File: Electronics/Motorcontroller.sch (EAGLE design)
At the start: 27 parts, among them Q1 IRFZ48V, Q2 IRF4905V, Q3 IRFZ48V, Q4 IRF4905V, Q5 IRFZ48V, Q6 IRF4905V, Q7 IRFZ48V, Q8 IRF4905V, X3 24V Batt

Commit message: Motorboard v2.0
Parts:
- added LED2, LED3, LED4, LED5: (no value), led:LED3MM
- added R7, R8: 2.2k, rcl:R-EU_0207/10
- LED1: device led:LED5MM -> led:LED3MM
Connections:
- removed net N$1: Q5.D, Q6.D, X2-2.KL
- new net N$23: LED2.C, LED3.A, R7.2
- new net N$24: LED4.A, LED5.C, R8.2
- new net N$25: LED4.C, LED5.A, Q5.D, Q6.D, X2-2.KL
- net N$18: now also R8.1
- net N$2: now also R7.1
- net N$4: now also LED2.A, LED3.C
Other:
- moved on the sheet: X1-1, X1-2, X2-1, X2-2
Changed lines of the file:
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@@
 <?xml version="1.0" encoding="utf-8"?>
 <!DOCTYPE eagle SYSTEM "eagle.dtd">
-<eagle version="6.0">
+<eagle version="6.1">
 <drawing>
 <settings>
@@
 <part name="P+5" library="supply1" deviceset="+24V" device=""/>
 <part name="R13" library="rcl" deviceset="R-EU_" device="0207/10" value="1k"/>
-<part name="LED1" library="led" deviceset="LED" device="5MM"/>
+<part name="LED1" library="led" deviceset="LED" device="3MM"/>
 <part name="OK1" library="optocoupler" deviceset="4N35" device=""/>
 <part name="OK2" library="optocoupler" deviceset="4N35" device=""/>
@@
 <part name="GND1" library="supply1" deviceset="GND" device=""/>
 <part name="C1" library="rcl" deviceset="CPOL-EU" device="E5-13" value="2200µF"/>
+<part name="LED2" library="led" deviceset="LED" device="3MM"/>
+<part name="LED3" library="led" deviceset="LED" device="3MM"/>
+<part name="R7" library="rcl" deviceset="R-EU_" device="0207/10" value="2.2k"/>
+<part name="LED4" library="led" deviceset="LED" device="3MM"/>
+<part name="LED5" library="led" deviceset="LED" device="3MM"/>
+<part name="R8" library="rcl" deviceset="R-EU_" device="0207/10" value="2.2k"/>
 </parts>
 <sheets>
@@
 <instance part="Q3" gate="G$1" x="190.5" y="93.98"/>
 <instance part="Q4" gate="G$1" x="190.5" y="109.22"/>
-<instance part="X1" gate="-1" x="226.06" y="101.6" rot="R180"/>
-<instance part="X1" gate="-2" x="226.06" y="104.14" rot="R180"/>
+<instance part="X1" gate="-1" x="246.38" y="101.6" rot="R180"/>
+<instance part="X1" gate="-2" x="246.38" y="104.14" rot="R180"/>
 <instance part="Q1" gate="G$1" x="215.9" y="93.98"/>
 <instance part="Q2" gate="G$1" x="215.9" y="109.22"/>
@@
 <instance part="Q5" gate="G$1" x="190.5" y="45.72"/>
 <instance part="Q6" gate="G$1" x="190.5" y="60.96"/>
-<instance part="X2" gate="-1" x="226.06" y="53.34" rot="R180"/>
-<instance part="X2" gate="-2" x="226.06" y="55.88" rot="R180"/>
+<instance part="X2" gate="-1" x="246.38" y="53.34" rot="R180"/>
+<instance part="X2" gate="-2" x="246.38" y="55.88" rot="R180"/>
 <instance part="Q7" gate="G$1" x="215.9" y="45.72"/>
 <instance part="Q8" gate="G$1" x="215.9" y="63.5"/>
@@
 <instance part="GND1" gate="1" x="142.24" y="68.58"/>
 <instance part="C1" gate="G$1" x="185.42" y="160.02"/>
+<instance part="LED2" gate="G$1" x="236.22" y="124.46"/>
+<instance part="LED3" gate="G$1" x="228.6" y="121.92" rot="R180"/>
+<instance part="R7" gate="G$1" x="236.22" y="111.76" rot="R90"/>
+<instance part="LED4" gate="G$1" x="228.6" y="73.66" rot="R180"/>
+<instance part="LED5" gate="G$1" x="236.22" y="76.2"/>
+<instance part="R8" gate="G$1" x="236.22" y="63.5" rot="R90"/>
 </instances>
 <busses>
@@
 <pinref part="X1" gate="-1" pin="KL"/>
 <wire x1="193.04" y1="101.6" x2="193.04" y2="99.06" width="0.1524" layer="91"/>
-<wire x1="220.98" y1="101.6" x2="193.04" y2="101.6" width="0.1524" layer="91"/>
+<wire x1="241.3" y1="101.6" x2="236.22" y2="101.6" width="0.1524" layer="91"/>
 <junction x="193.04" y="101.6"/>
+<pinref part="R7" gate="G$1" pin="1"/>
+<wire x1="236.22" y1="101.6" x2="193.04" y2="101.6" width="0.1524" layer="91"/>
+<wire x1="236.22" y1="106.68" x2="236.22" y2="101.6" width="0.1524" layer="91"/>
+<junction x="236.22" y="101.6"/>
 </segment>
 </net>
@@
 <wire x1="218.44" y1="104.14" x2="218.44" y2="99.06" width="0.1524" layer="91"/>
 <pinref part="X1" gate="-2" pin="KL"/>
-<wire x1="220.98" y1="104.14" x2="218.44" y2="104.14" width="0.1524" layer="91"/>
+<wire x1="241.3" y1="104.14" x2="238.76" y2="104.14" width="0.1524" layer="91"/>
 <junction x="218.44" y="104.14"/>
+<wire x1="238.76" y1="104.14" x2="218.44" y2="104.14" width="0.1524" layer="91"/>
+<wire x1="238.76" y1="104.14" x2="238.76" y2="129.54" width="0.1524" layer="91"/>
+<junction x="238.76" y="104.14"/>
+<pinref part="LED3" gate="G$1" pin="C"/>
+<wire x1="228.6" y1="127" x2="228.6" y2="129.54" width="0.1524" layer="91"/>
+<wire x1="228.6" y1="129.54" x2="236.22" y2="129.54" width="0.1524" layer="91"/>
+<pinref part="LED2" gate="G$1" pin="A"/>
+<wire x1="236.22" y1="129.54" x2="238.76" y2="129.54" width="0.1524" layer="91"/>
+<wire x1="236.22" y1="127" x2="236.22" y2="129.54" width="0.1524" layer="91"/>
+<junction x="236.22" y="129.54"/>
 </segment>
 </net>
@@
 </segment>
 </net>
-<net name="N$1" class="0">
-<segment>
-<pinref part="Q5" gate="G$1" pin="D"/>
-<pinref part="Q6" gate="G$1" pin="D"/>
-<wire x1="193.04" y1="55.88" x2="193.04" y2="50.8" width="0.1524" layer="91"/>
-<pinref part="X2" gate="-2" pin="KL"/>
-<wire x1="220.98" y1="55.88" x2="193.04" y2="55.88" width="0.1524" layer="91"/>
-<junction x="193.04" y="55.88"/>
-</segment>
-</net>
 <net name="N$18" class="0">
 <segment>
@@
 <pinref part="X2" gate="-1" pin="KL"/>
 <wire x1="218.44" y1="53.34" x2="218.44" y2="50.8" width="0.1524" layer="91"/>
-<wire x1="220.98" y1="53.34" x2="218.44" y2="53.34" width="0.1524" layer="91"/>
+<wire x1="241.3" y1="53.34" x2="236.22" y2="53.34" width="0.1524" layer="91"/>
 <junction x="218.44" y="53.34"/>
+<pinref part="R8" gate="G$1" pin="1"/>
+<wire x1="236.22" y1="53.34" x2="218.44" y2="53.34" width="0.1524" layer="91"/>
+<wire x1="236.22" y1="58.42" x2="236.22" y2="53.34" width="0.1524" layer="91"/>
+<junction x="236.22" y="53.34"/>
 </segment>
 </net>
@@
 </segment>
 </net>
+<net name="N$23" class="0">
+<segment>
+<pinref part="LED3" gate="G$1" pin="A"/>
+<wire x1="228.6" y1="119.38" x2="228.6" y2="116.84" width="0.1524" layer="91"/>
+<pinref part="R7" gate="G$1" pin="2"/>
+<wire x1="228.6" y1="116.84" x2="236.22" y2="116.84" width="0.1524" layer="91"/>
+<pinref part="LED2" gate="G$1" pin="C"/>
+<wire x1="236.22" y1="119.38" x2="236.22" y2="116.84" width="0.1524" layer="91"/>
+<junction x="236.22" y="116.84"/>
+</segment>
+</net>
+<net name="N$24" class="0">
+<segment>
+<pinref part="R8" gate="G$1" pin="2"/>
+<pinref part="LED5" gate="G$1" pin="C"/>
+<wire x1="236.22" y1="68.58" x2="236.22" y2="71.12" width="0.1524" layer="91"/>
+<pinref part="LED4" gate="G$1" pin="A"/>
+<wire x1="236.22" y1="68.58" x2="228.6" y2="68.58" width="0.1524" layer="91"/>
+<wire x1="228.6" y1="68.58" x2="228.6" y2="71.12" width="0.1524" layer="91"/>
+<junction x="236.22" y="68.58"/>
+</segment>
+</net>
+<net name="N$25" class="0">
+<segment>
+<pinref part="LED4" gate="G$1" pin="C"/>
+<wire x1="228.6" y1="78.74" x2="228.6" y2="81.28" width="0.1524" layer="91"/>
+<wire x1="238.76" y1="81.28" x2="236.22" y2="81.28" width="0.1524" layer="91"/>
+<pinref part="LED5" gate="G$1" pin="A"/>
+<wire x1="236.22" y1="81.28" x2="228.6" y2="81.28" width="0.1524" layer="91"/>
+<wire x1="236.22" y1="78.74" x2="236.22" y2="81.28" width="0.1524" layer="91"/>
+<junction x="236.22" y="81.28"/>
+<pinref part="Q5" gate="G$1" pin="D"/>
+<pinref part="Q6" gate="G$1" pin="D"/>
+<wire x1="193.04" y1="55.88" x2="193.04" y2="50.8" width="0.1524" layer="91"/>
+<pinref part="X2" gate="-2" pin="KL"/>
+<wire x1="241.3" y1="55.88" x2="238.76" y2="55.88" width="0.1524" layer="91"/>
+<junction x="193.04" y="55.88"/>
+<wire x1="238.76" y1="55.88" x2="193.04" y2="55.88" width="0.1524" layer="91"/>
+<wire x1="238.76" y1="81.28" x2="238.76" y2="55.88" width="0.1524" layer="91"/>
+<junction x="238.76" y="55.88"/>
+</segment>
+</net>

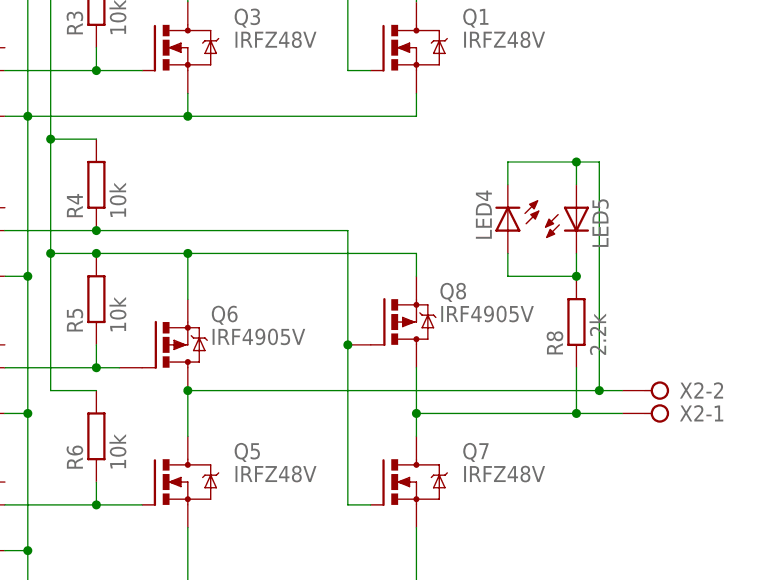
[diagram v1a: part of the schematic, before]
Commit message: Updated .sch to be consisting to .brd (it was missing from the last commit)
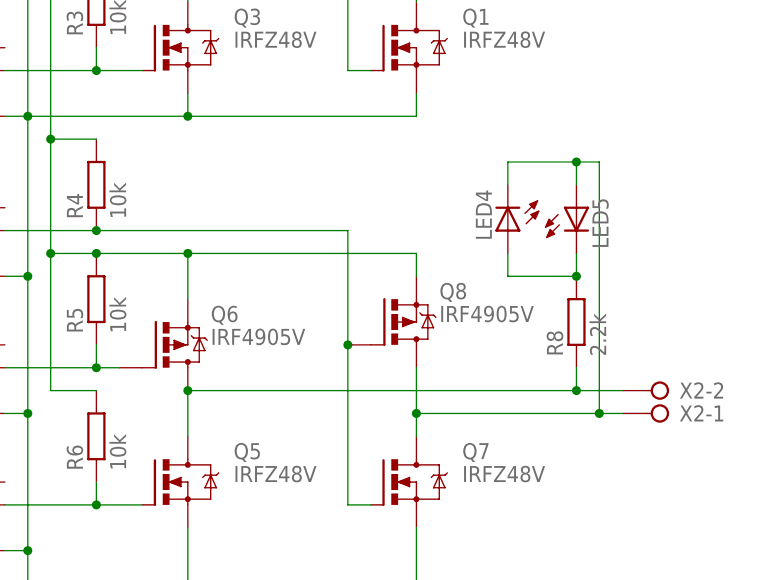
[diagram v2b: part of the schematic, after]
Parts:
- R7, R8: device rcl:R-EU_0207/10 -> rcl:R-EU_0207/7
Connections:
- removed net N$18: Q7.D, Q8.D, R8.1, X2-1.KL
- new net N$1: LED4.C, LED5.A, Q7.D, Q8.D, X2-1.KL
- net N$25: now also R8.1; no longer LED4.C, LED5.A
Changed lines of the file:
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@@
 <part name="LED2" library="led" deviceset="LED" device="3MM"/>
 <part name="LED3" library="led" deviceset="LED" device="3MM"/>
-<part name="R7" library="rcl" deviceset="R-EU_" device="0207/10" value="2.2k"/>
+<part name="R7" library="rcl" deviceset="R-EU_" device="0207/7" value="2.2k"/>
 <part name="LED4" library="led" deviceset="LED" device="3MM"/>
 <part name="LED5" library="led" deviceset="LED" device="3MM"/>
-<part name="R8" library="rcl" deviceset="R-EU_" device="0207/10" value="2.2k"/>
+<part name="R8" library="rcl" deviceset="R-EU_" device="0207/7" value="2.2k"/>
 </parts>
 <sheets>
@@
 </segment>
 </net>
-<net name="N$18" class="0">
-<segment>
-<pinref part="Q8" gate="G$1" pin="D"/>
-<pinref part="Q7" gate="G$1" pin="D"/>
-<wire x1="218.44" y1="58.42" x2="218.44" y2="53.34" width="0.1524" layer="91"/>
-<pinref part="X2" gate="-1" pin="KL"/>
-<wire x1="218.44" y1="53.34" x2="218.44" y2="50.8" width="0.1524" layer="91"/>
-<wire x1="241.3" y1="53.34" x2="236.22" y2="53.34" width="0.1524" layer="91"/>
-<junction x="218.44" y="53.34"/>
-<pinref part="R8" gate="G$1" pin="1"/>
-<wire x1="236.22" y1="53.34" x2="218.44" y2="53.34" width="0.1524" layer="91"/>
-<wire x1="236.22" y1="58.42" x2="236.22" y2="53.34" width="0.1524" layer="91"/>
-<junction x="236.22" y="53.34"/>
-</segment>
-</net>
 <net name="N$19" class="0">
 <segment>
@@
 <net name="N$25" class="0">
 <segment>
-<pinref part="LED4" gate="G$1" pin="C"/>
-<wire x1="228.6" y1="78.74" x2="228.6" y2="81.28" width="0.1524" layer="91"/>
-<wire x1="238.76" y1="81.28" x2="236.22" y2="81.28" width="0.1524" layer="91"/>
-<pinref part="LED5" gate="G$1" pin="A"/>
-<wire x1="236.22" y1="81.28" x2="228.6" y2="81.28" width="0.1524" layer="91"/>
-<wire x1="236.22" y1="78.74" x2="236.22" y2="81.28" width="0.1524" layer="91"/>
-<junction x="236.22" y="81.28"/>
 <pinref part="Q5" gate="G$1" pin="D"/>
 <pinref part="Q6" gate="G$1" pin="D"/>
 <wire x1="193.04" y1="55.88" x2="193.04" y2="50.8" width="0.1524" layer="91"/>
 <pinref part="X2" gate="-2" pin="KL"/>
-<wire x1="241.3" y1="55.88" x2="238.76" y2="55.88" width="0.1524" layer="91"/>
 <junction x="193.04" y="55.88"/>
-<wire x1="238.76" y1="55.88" x2="193.04" y2="55.88" width="0.1524" layer="91"/>
-<wire x1="238.76" y1="81.28" x2="238.76" y2="55.88" width="0.1524" layer="91"/>
-<junction x="238.76" y="55.88"/>
-</segment>
-</net>
+<wire x1="241.3" y1="55.88" x2="236.22" y2="55.88" width="0.1524" layer="91"/>
+<pinref part="R8" gate="G$1" pin="1"/>
+<wire x1="236.22" y1="55.88" x2="193.04" y2="55.88" width="0.1524" layer="91"/>
+<wire x1="236.22" y1="58.42" x2="236.22" y2="55.88" width="0.1524" layer="91"/>
+<junction x="236.22" y="55.88"/>
+</segment>
+</net>
+<net name="N$1" class="0">
+<segment>
+<wire x1="238.76" y1="81.28" x2="236.22" y2="81.28" width="0.1524" layer="91"/>
+<pinref part="LED5" gate="G$1" pin="A"/>
+<wire x1="236.22" y1="78.74" x2="236.22" y2="81.28" width="0.1524" layer="91"/>
+<junction x="236.22" y="81.28"/>
+<wire x1="236.22" y1="81.28" x2="228.6" y2="81.28" width="0.1524" layer="91"/>
+<pinref part="LED4" gate="G$1" pin="C"/>
+<wire x1="228.6" y1="78.74" x2="228.6" y2="81.28" width="0.1524" layer="91"/>
+<pinref part="Q8" gate="G$1" pin="D"/>
+<pinref part="Q7" gate="G$1" pin="D"/>
+<wire x1="218.44" y1="58.42" x2="218.44" y2="53.34" width="0.1524" layer="91"/>
+<pinref part="X2" gate="-1" pin="KL"/>
+<wire x1="218.44" y1="53.34" x2="218.44" y2="50.8" width="0.1524" layer="91"/>
+<junction x="218.44" y="53.34"/>
+<wire x1="241.3" y1="53.34" x2="238.76" y2="53.34" width="0.1524" layer="91"/>
+<wire x1="238.76" y1="53.34" x2="218.44" y2="53.34" width="0.1524" layer="91"/>
+<wire x1="238.76" y1="81.28" x2="238.76" y2="53.34" width="0.1524" layer="91"/>
+<junction x="238.76" y="53.34"/>
+</segment>
+</net>

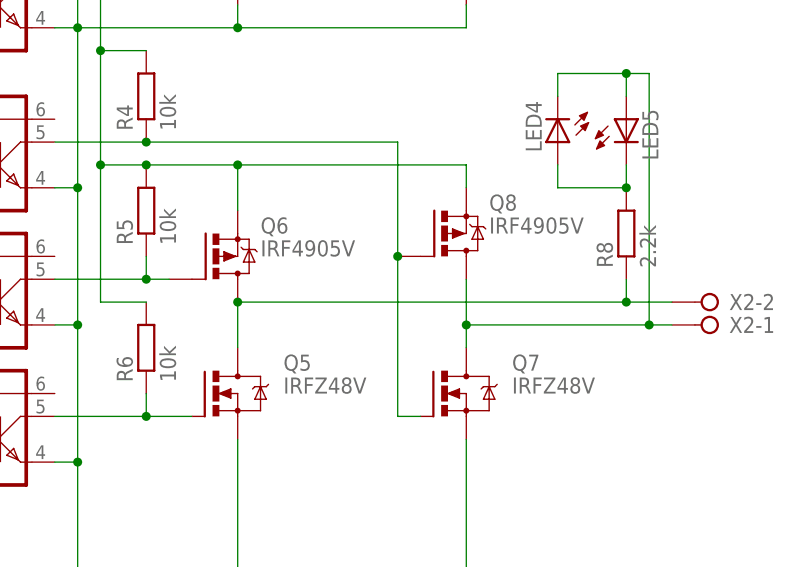
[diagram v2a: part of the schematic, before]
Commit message: Renamed HEXFETs so both bridge fit
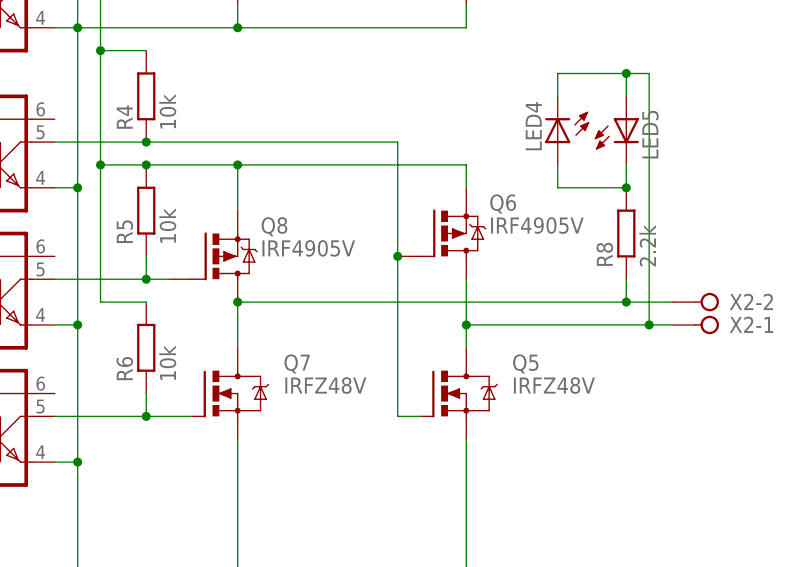
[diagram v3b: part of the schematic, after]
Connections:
- net N$1: now also Q5.D, Q6.D; no longer Q7.D, Q8.D
- net N$19: now also Q5.G, Q6.G; no longer Q7.G, Q8.G
- net N$21: now also Q8.G; no longer Q6.G
- net N$22: now also Q7.G; no longer Q5.G
- net N$25: now also Q7.D, Q8.D; no longer Q5.D, Q6.D
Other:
- moved on the sheet: Q5, Q6, Q7, Q8
